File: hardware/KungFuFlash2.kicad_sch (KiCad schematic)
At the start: 52 parts, among them J1 SWD, J2 USB_B_Micro, J3 Wifi, Q1 BC817, SW1 Reset, SW2 Menu, SW3 Special, U1 C64-Exp-Port, U2 AMS1117-3.3, U3 STM32H7B0VBTx, Y1 25MHz

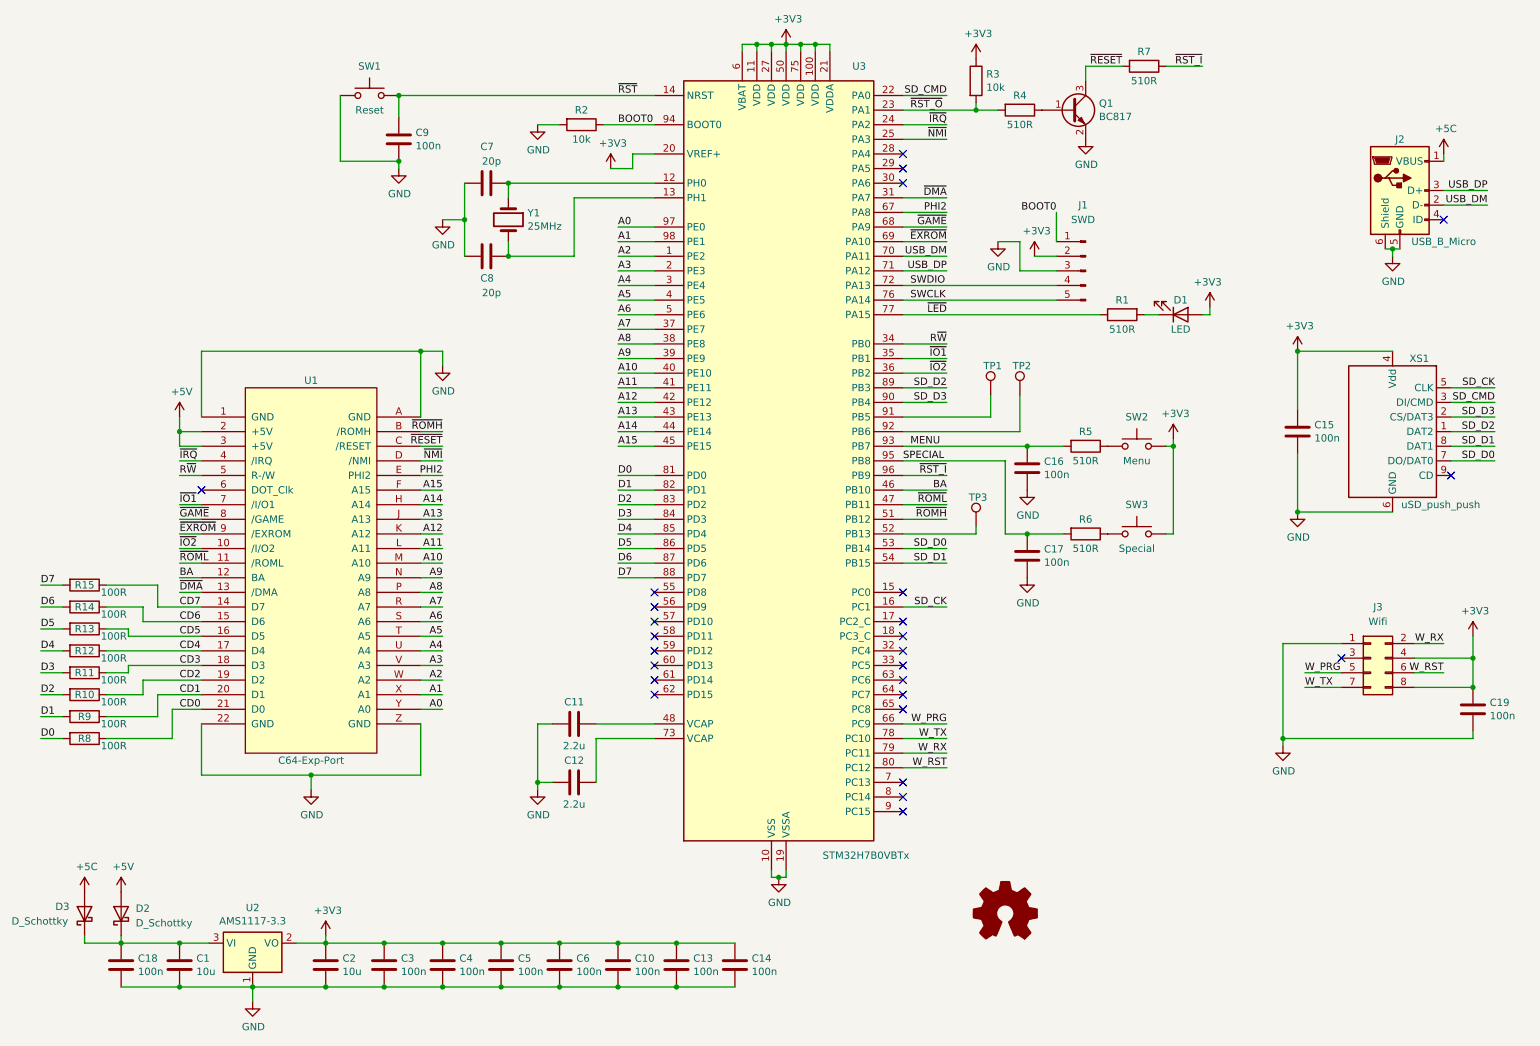
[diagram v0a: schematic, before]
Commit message: Adapting board for JLCPCB ordering
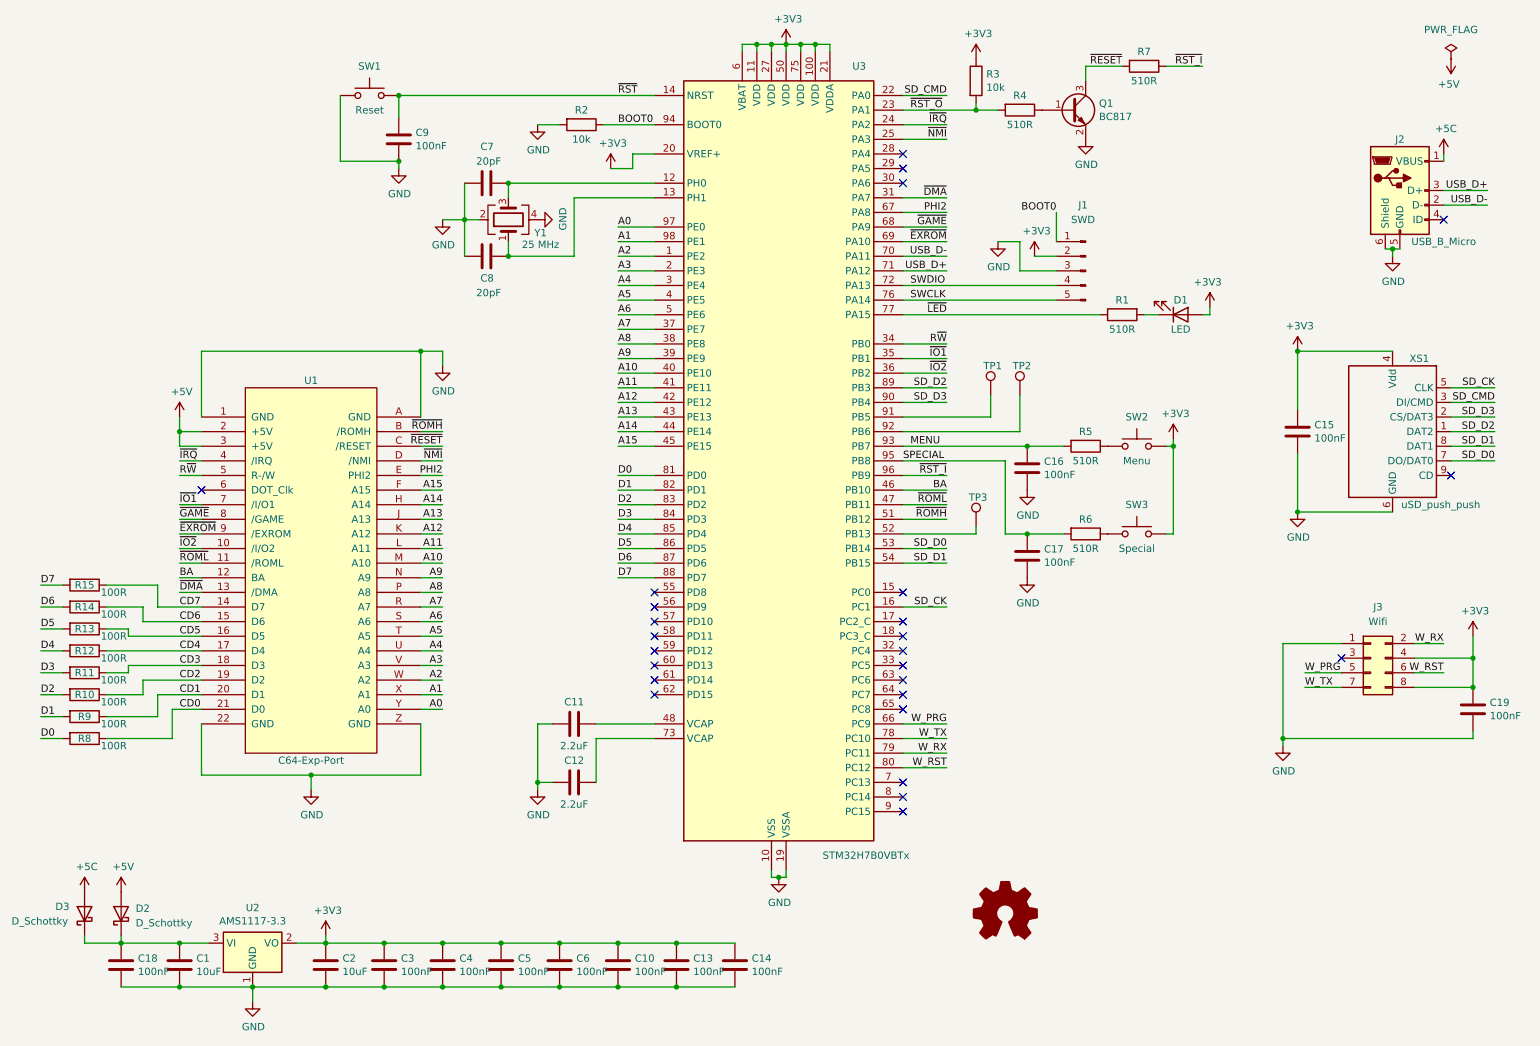
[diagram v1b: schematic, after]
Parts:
- removed Y1: 25MHz, Crystal:Crystal_SMD_5032-2Pin_5.0x3.2mm, symbol Device:Crystal
- added Y1: 25 MHz, Crystal:Crystal_SMD_3225-4Pin_3.2x2.5mm, symbol Device:Crystal_GND24
- C1, C2: value 10u -> 10uF; LCSC Part # (none) -> C15850
- C10, C13, C14, C15, C16, C17, C18, C19, C3, C4, C5, C6, C9: value 100n -> 100nF; LCSC Part # (none) -> C14663
- C11, C12: value 2.2u -> 2.2uF; LCSC Part # (none) -> C377773
- C7, C8: value 20p -> 20pF; LCSC Part # (none) -> C1648
- D1: LCSC Part # (none) -> C2297
- D2, D3: LCSC Part # (none) -> C14996
- J2: footprint KungFuFlash2:Conn_USBmicro-B_ebay-side_TH -> mod:Conn_USBmini_reichelt
- Q1: LCSC Part # (none) -> C466643
- R1, R4, R5, R6, R7: LCSC Part # (none) -> C17734
- R10, R11, R12, R13, R14, R15, R8, R9: LCSC Part # (none) -> C17408
- R2, R3: LCSC Part # (none) -> C17414
- U2: LCSC Part # (none) -> C6186
- U3: LCSC Part # (none) -> C730227
- XS1: LCSC Part # (none) -> C91145
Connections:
- net GND: now also Y1.2, Y1.4
- net at C7.2, U3.12 (PH0): now also Y1.3
- net at C8.2, U3.13 (PH1): now also Y1.1
- net USB_DM renamed USB_D-
- net USB_DP renamed USB_D+
